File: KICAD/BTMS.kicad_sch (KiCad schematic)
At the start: 152 parts, among them J1 Batt_Ballance, J2 AUX_Charge, J3 Battery_IO, J4 Power_Out, J5 BT_LM62, J6 DSKY, J7 PWR_SW, J8 ICSP, J9 Heater, P1 USB_C_Plug, Q1 SSM3K341R, Q2 DMN65D8L, Q3 SSM3K341R, Q4 FDN340P, Q5 FDN340P, Q6 FDN340P, Q7 DMN65D8L, Q8 DMN65D8L, SW1 PTS526, U1 ACS711xLCTR-25AB, U10 BA033CC0FP-E2, U11 AON7522E, U12 AON7522E, U13 LM62CIM3/NOPB, U14 FAN3100TSX, U15 FAN3100TSX, U16 AON7522E, U17 dsPIC30F3011-PT, U18 FT230XQ, U2 AP33771, U3 IS281-4, U4 Q294700DSGR, U5 SCF4030-12-0X, U6 AONR21321, U7 ACS711xLCTR-25AB, U8 IS281-4, U9 IRS2184

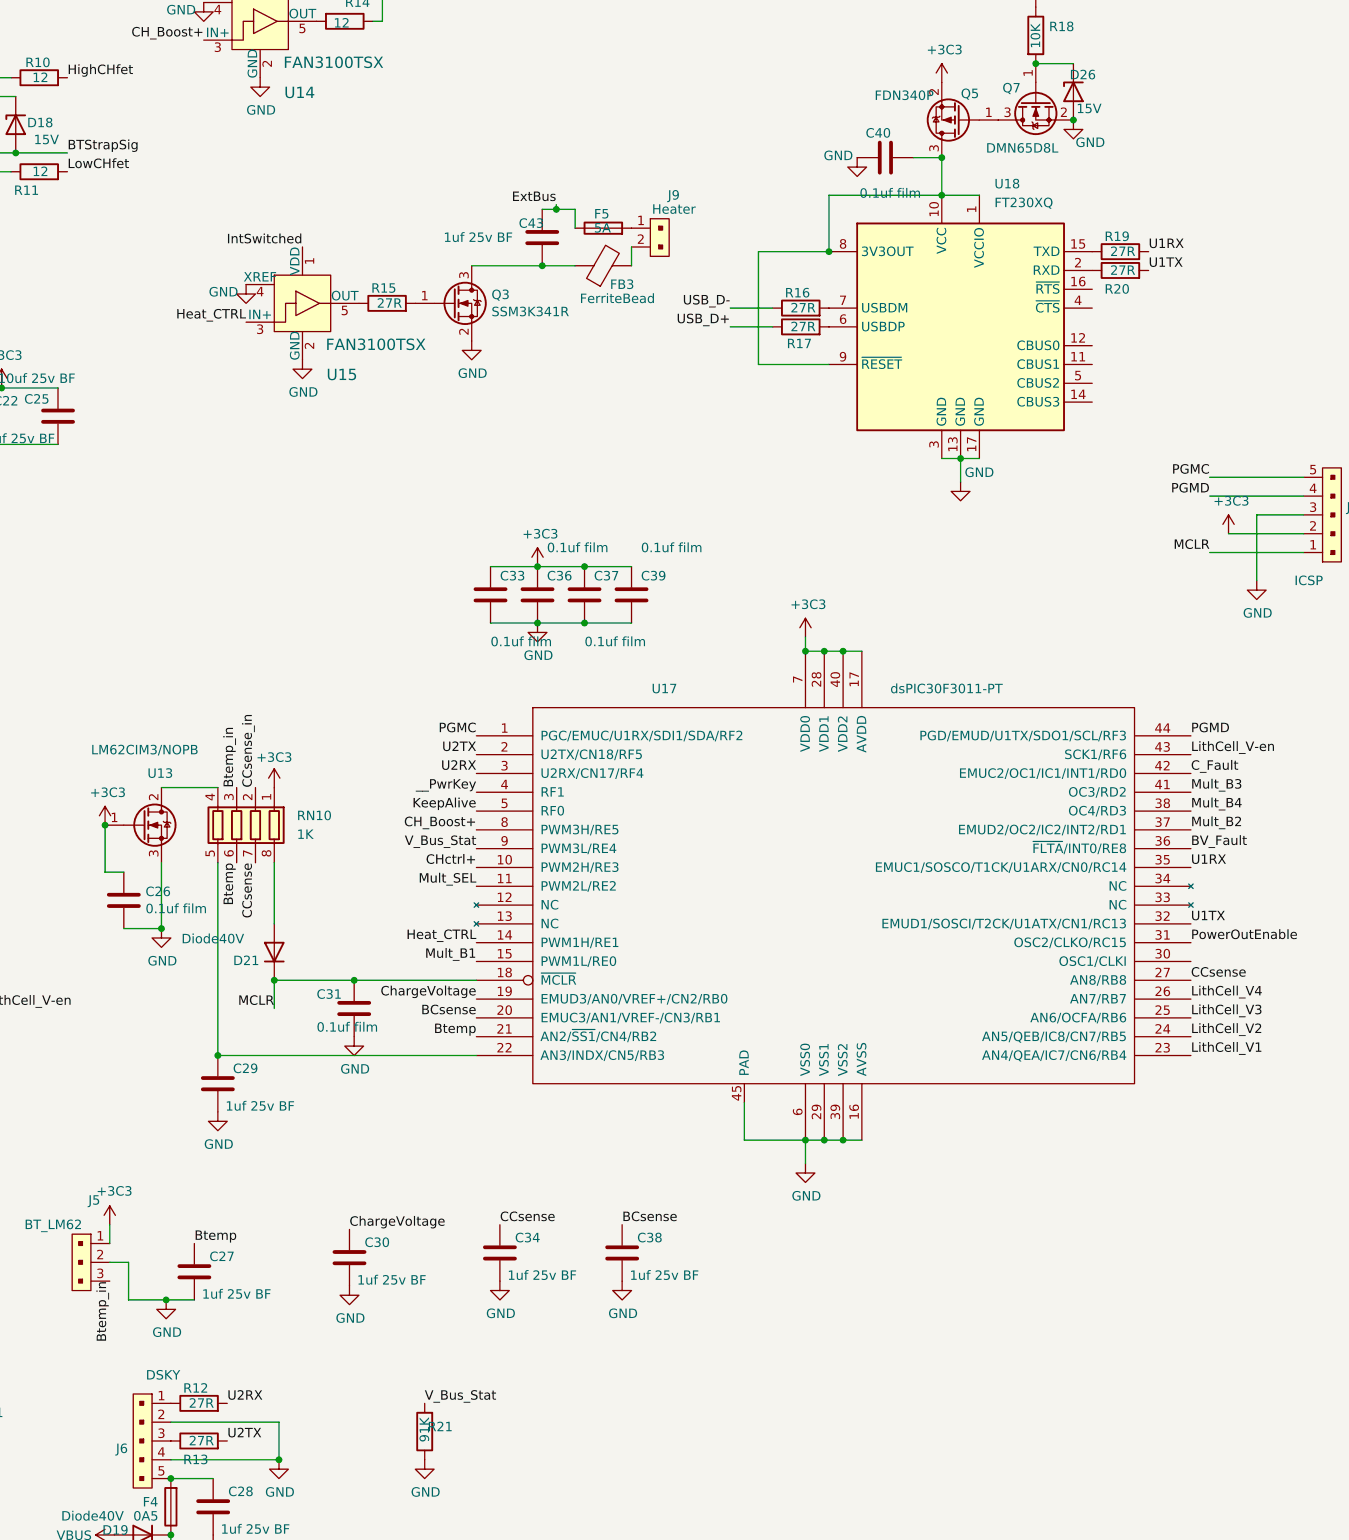
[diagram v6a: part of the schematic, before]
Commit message: Added 10K pullup resistors to dsPIC's serial RX lines.
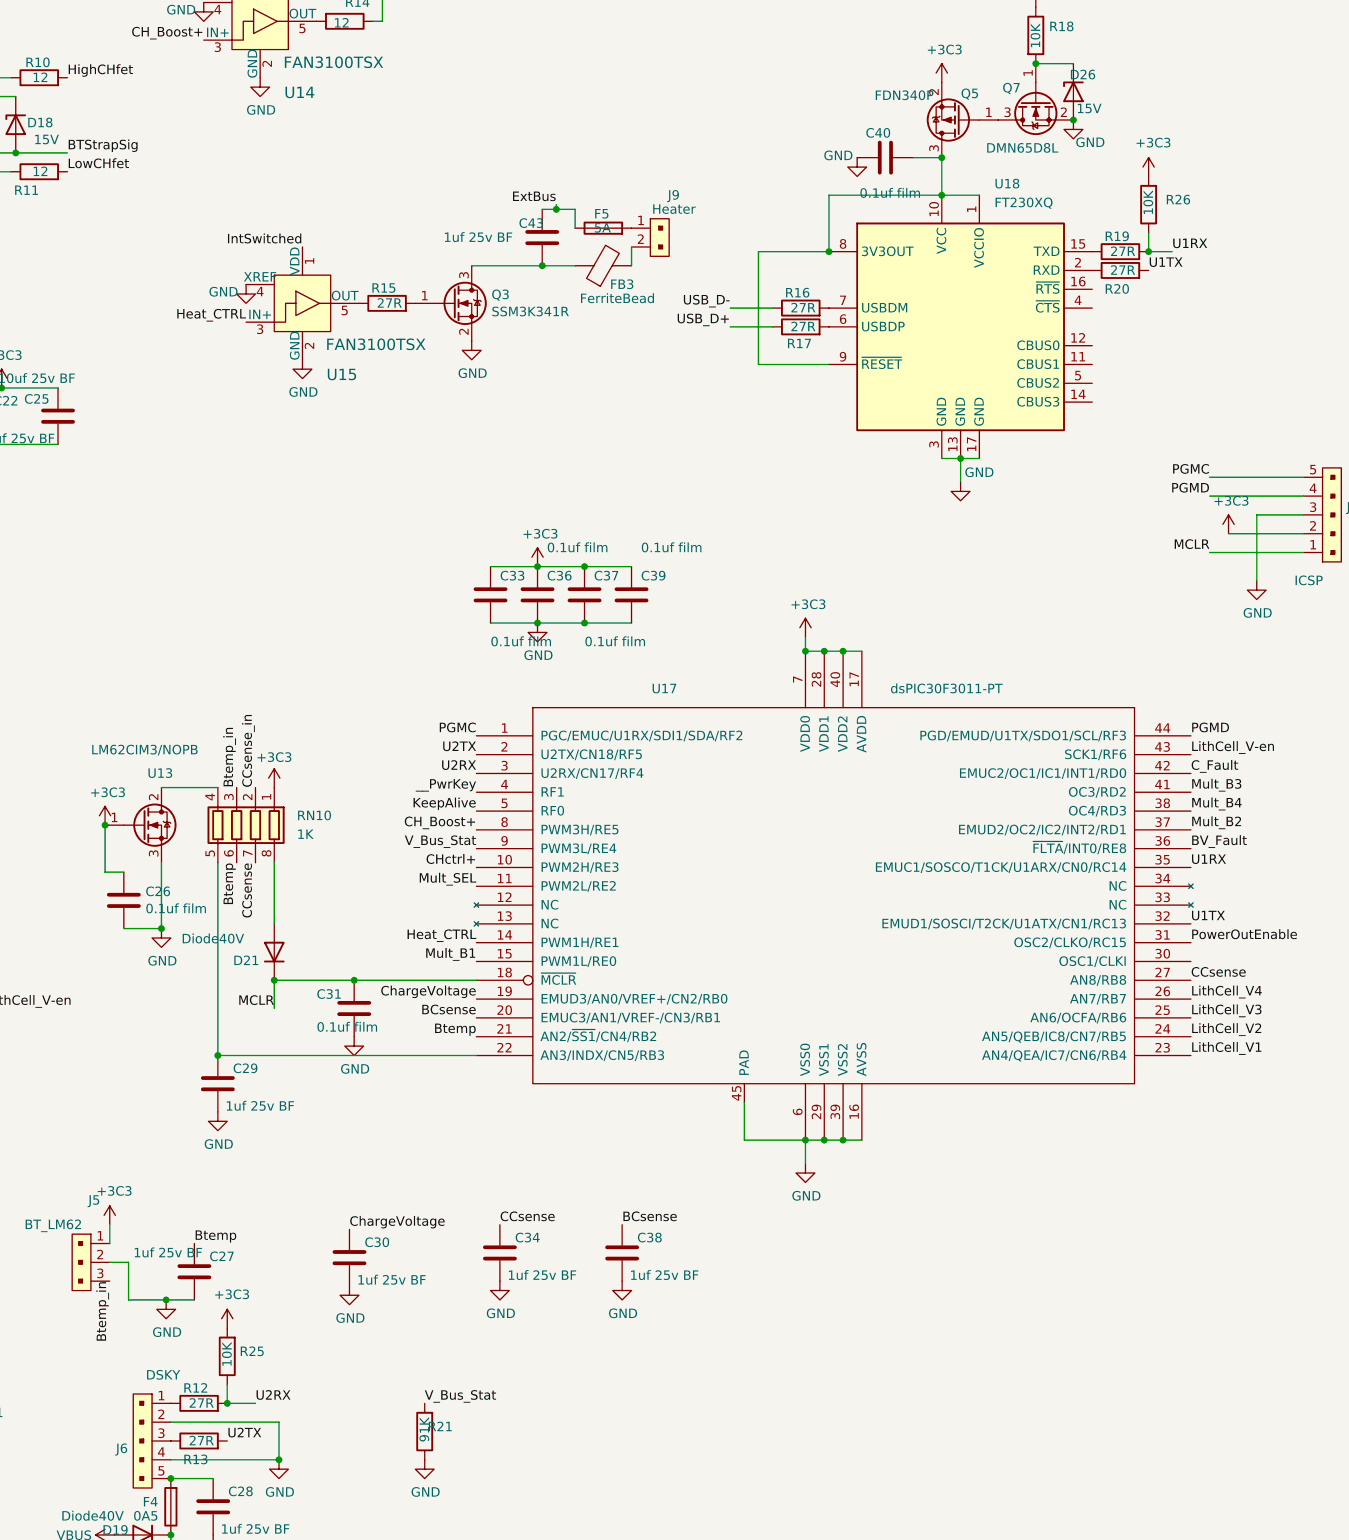
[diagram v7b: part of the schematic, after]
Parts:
- added R25, R26: 10K, Resistor_SMD:R_0603_1608Metric, symbol Device:R
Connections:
- net +5C: now also R25.2, R26.2
- net U1RX: now also R26.1
- net U2RX: now also R25.1
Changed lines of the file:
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@@
   (junction (at 94.615 102.235) (diameter 0) (color 0 0 0 0)
   )
+  (junction (at 250.825 257.175) (diameter 0) (color 0 0 0 0)
+  )
   (junction (at 77.47 31.115) (diameter 0) (color 0 0 0 0)
   )
@@
   (junction (at 331.47 221.615) (diameter 0) (color 0 0 0 0)
   )
+  (junction (at 375.285 101.6) (diameter 0) (color 0 0 0 0)
+  )
   (junction (at 194.945 127.635) (diameter 0) (color 0 0 0 0)
   )
@@
     (stroke (width 0) (type default) (color 0 0 0 0))
   )
+  (wire (pts (xy 250.825 257.175) (xy 254.635 257.175))
+    (stroke (width 0) (type default) (color 0 0 0 0))
+  )
   (wire (pts (xy 100.33 66.675) (xy 100.33 71.755))
     (stroke (width 0) (type default) (color 0 0 0 0))
@@
     (stroke (width 0) (type default) (color 0 0 0 0))
   )
+  (wire (pts (xy 250.825 254.635) (xy 250.825 257.175))
+    (stroke (width 0) (type default) (color 0 0 0 0))
+  )
   (wire (pts (xy 97.79 24.765) (xy 102.87 24.765))
     (stroke (width 0) (type default) (color 0 0 0 0))
@@
     (stroke (width 0) (type default) (color 0 0 0 0))
   )
+  (wire (pts (xy 375.285 99.06) (xy 375.285 101.6))
+    (stroke (width 0) (type default) (color 0 0 0 0))
+  )
   (wire (pts (xy 184.785 149.225) (xy 184.785 151.13))
     (stroke (width 0) (type default) (color 0 0 0 0))
@@
     (stroke (width 0) (type default) (color 0 0 0 0))
   )
+  (wire (pts (xy 375.285 101.6) (xy 378.46 101.6))
+    (stroke (width 0) (type default) (color 0 0 0 0))
+  )
   (wire (pts (xy 87.63 66.675) (xy 87.63 67.945))
     (stroke (width 0) (type default) (color 0 0 0 0))
@@
     (effects (font (size 1.27 1.27)) (justify left bottom))
   )
-  (label "U2RX" (at 250.825 257.175 0)
+  (label "U2RX" (at 254.635 257.175 0)
     (effects (font (size 1.27 1.27)) (justify left bottom))
   )
@@
     (effects (font (size 1.27 1.27)) (justify right bottom))
   )
-  (label "U1RX" (at 375.285 101.6 0)
+  (label "U1RX" (at 378.46 101.6 0)
     (effects (font (size 1.27 1.27)) (justify left bottom))
   )
@@
     (pin "1")
   )
+  (symbol (lib_id "power:+5C") (at 375.285 91.44 0) (unit 1)
+    (in_bom yes) (on_board yes)
+    (property "Reference" "#PWR0108" (id 0) (at 375.285 95.25 0)
+      (effects (font (size 1.27 1.27)) hide)
+    )
+    (property "Value" "+3C3" (id 1) (at 375.92 86.9188 0))
+    (property "Footprint" "" (id 2) (at 375.285 91.44 0)
+      (effects (font (size 1.27 1.27)) hide)
+    )
+    (property "Datasheet" "" (id 3) (at 375.285 91.44 0)
+      (effects (font (size 1.27 1.27)) hide)
+    )
+    (pin "1")
+  )
   (symbol (lib_id "Device:D_Schottky") (at 211.455 66.675 180) (unit 1)
     (in_bom yes) (on_board yes)
@@
     (pin "2")
   )
+  (symbol (lib_id "Device:R") (at 250.825 250.825 180) (unit 1)
+    (in_bom yes) (on_board yes)
+    (property "Reference" "R25" (id 0) (at 255.905 250.19 0)
+      (effects (font (size 1.27 1.27)) (justify left))
+    )
+    (property "Value" "10K" (id 1) (at 250.825 248.92 90)
+      (effects (font (size 1.27 1.27)) (justify left))
+    )
+    (property "Footprint" "Resistor_SMD:R_0603_1608Metric" (id 2) (at 252.603 250.825 90)
+      (effects (font (size 1.27 1.27)) hide)
+    )
+    (property "Datasheet" "~" (id 3) (at 250.825 250.825 0)
+      (effects (font (size 1.27 1.27)) hide)
+    )
+    (property "DK_Detail_Page" "https://www.digikey.com/en/products/detail/bourns-inc/CR0603-FX-1002ELF/3593188" (id 4) (at 250.825 250.825 0)
+      (effects (font (size 1.27 1.27)) hide)
+    )
+    (property "Digi-Key_PN" "CR0603-FX-1002ELFCT-ND" (id 5) (at 250.825 250.825 0)
+      (effects (font (size 1.27 1.27)) hide)
+    )
+    (pin "1")
+    (pin "2")
+  )
   (symbol (lib_id "power:GND") (at 57.785 36.195 90) (unit 1)
     (in_bom yes) (on_board yes)
@@
     (pin "2")
   )
+  (symbol (lib_id "power:+5C") (at 250.825 247.015 0) (unit 1)
+    (in_bom yes) (on_board yes)
+    (property "Reference" "#PWR0107" (id 0) (at 250.825 250.825 0)
+      (effects (font (size 1.27 1.27)) hide)
+    )
+    (property "Value" "+3C3" (id 1) (at 251.46 242.4938 0))
+    (property "Footprint" "" (id 2) (at 250.825 247.015 0)
+      (effects (font (size 1.27 1.27)) hide)
+    )
+    (property "Datasheet" "" (id 3) (at 250.825 247.015 0)
+      (effects (font (size 1.27 1.27)) hide)
+    )
+    (pin "1")
+  )
   (symbol (lib_id "power:GND") (at 200.66 35.56 0) (unit 1)
     (in_bom yes) (on_board yes)
@@
       (effects (font (size 1.27 1.27)) (justify left))
     )
-    (property "Value" "1uf 25v BF" (id 1) (at 247.396 242.443 0)
+    (property "Value" "1uf 25v BF" (id 1) (at 238.125 236.855 0)
       (effects (font (size 1.27 1.27)) (justify left))
     )
@@
     (pin "2")
   )
+  (symbol (lib_id "Device:R") (at 375.285 95.25 180) (unit 1)
+    (in_bom yes) (on_board yes)
+    (property "Reference" "R26" (id 0) (at 381 94.615 0)
+      (effects (font (size 1.27 1.27)) (justify left))
+    )
+    (property "Value" "10K" (id 1) (at 375.285 93.345 90)
+      (effects (font (size 1.27 1.27)) (justify left))
+    )
+    (property "Footprint" "Resistor_SMD:R_0603_1608Metric" (id 2) (at 377.063 95.25 90)
+      (effects (font (size 1.27 1.27)) hide)
+    )
+    (property "Datasheet" "~" (id 3) (at 375.285 95.25 0)
+      (effects (font (size 1.27 1.27)) hide)
+    )
+    (property "DK_Detail_Page" "https://www.digikey.com/en/products/detail/bourns-inc/CR0603-FX-1002ELF/3593188" (id 4) (at 375.285 95.25 0)
+      (effects (font (size 1.27 1.27)) hide)
+    )
+    (property "Digi-Key_PN" "CR0603-FX-1002ELFCT-ND" (id 5) (at 375.285 95.25 0)
+      (effects (font (size 1.27 1.27)) hide)
+    )
+    (pin "1")
+    (pin "2")
+  )
   (symbol (lib_id "power:GND") (at 205.105 95.885 0) (unit 1)
     (in_bom yes) (on_board yes)
@@
       (reference "#PWR0106") (unit 1) (value "GND") (footprint "")
     )
+    (path "/7d4ee4ca-b006-446d-a3ac-c80b68e23b3d"
+      (reference "#PWR0107") (unit 1) (value "+3C3") (footprint "")
+    )
+    (path "/08dcb5c3-f129-4ec5-8278-3dc3347d58e2"
+      (reference "#PWR0108") (unit 1) (value "+3C3") (footprint "")
+    )
     (path "/64c76206-53c0-4f04-b9c5-7beac0937b65"
       (reference "C1") (unit 1) (value "0.1uf film") (footprint "Capacitor_SMD:C_0603_1608Metric")
@@
       (reference "R24") (unit 1) (value "10K") (footprint "Resistor_SMD:R_0603_1608Metric")
     )
+    (path "/25af85ed-4d99-4b06-810c-8020a57e613d"
+      (reference "R25") (unit 1) (value "10K") (footprint "Resistor_SMD:R_0603_1608Metric")
+    )
+    (path "/e72ebb1b-6dff-4341-94fe-9fc818944816"
+      (reference "R26") (unit 1) (value "10K") (footprint "Resistor_SMD:R_0603_1608Metric")
+    )
     (path "/6d1558b7-32bb-4234-9884-0300df2238db"

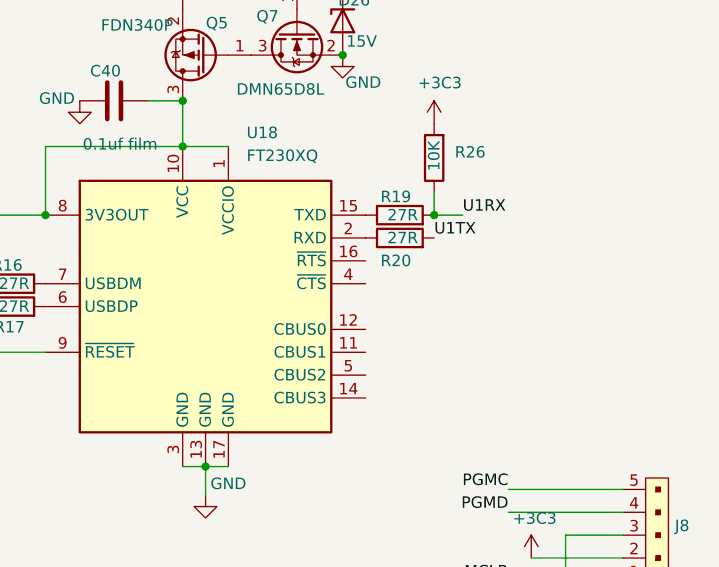
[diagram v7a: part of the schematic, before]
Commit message: Added ground connection to CTS pin on FTDI chip.
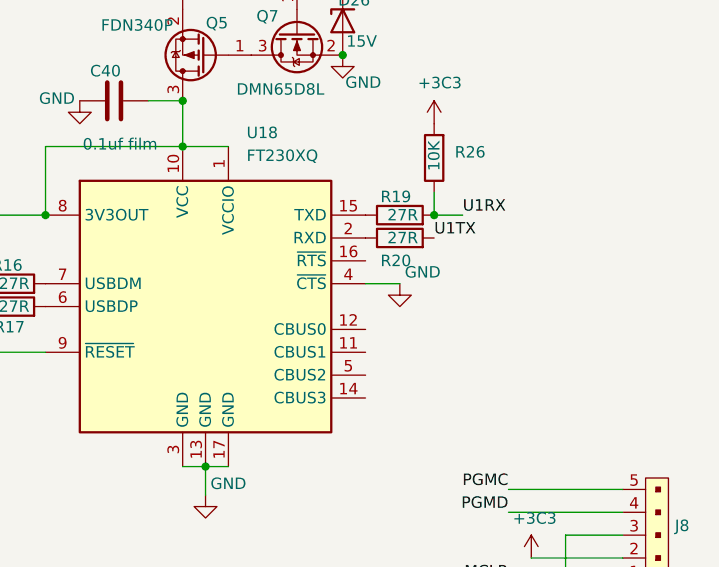
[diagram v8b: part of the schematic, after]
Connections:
- net GND: now also U18.4 (~{CTS})
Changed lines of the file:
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@@
     (stroke (width 0) (type default) (color 0 0 0 0))
   )
+  (wire (pts (xy 367.665 109.22) (xy 371.475 109.22))
+    (stroke (width 0) (type default) (color 0 0 0 0))
+  )
   (wire (pts (xy 396.24 139.7) (xy 386.08 139.7))
     (stroke (width 0) (type default) (color 0 0 0 0))
@@
     (pin "2")
   )
+  (symbol (lib_id "power:GND") (at 371.475 109.22 0) (unit 1)
+    (in_bom yes) (on_board yes)
+    (property "Reference" "#PWR?" (id 0) (at 371.475 115.57 0)
+      (effects (font (size 1.27 1.27)) hide)
+    )
+    (property "Value" "GND" (id 1) (at 374.015 107.95 0))
+    (property "Footprint" "" (id 2) (at 371.475 109.22 0)
+      (effects (font (size 1.27 1.27)) hide)
+    )
+    (property "Datasheet" "" (id 3) (at 371.475 109.22 0)
+      (effects (font (size 1.27 1.27)) hide)
+    )
+    (pin "1")
+  )
   (symbol (lib_id "Device:C") (at 161.925 29.21 0) (unit 1)
     (in_bom yes) (on_board yes)
@@
       (reference "#PWR0108") (unit 1) (value "+3C3") (footprint "")
     )
+    (path "/03e2ee64-2c01-41a8-b8e3-25bc34cb7229"
+      (reference "#PWR?") (unit 1) (value "GND") (footprint "")
+    )
     (path "/64c76206-53c0-4f04-b9c5-7beac0937b65"
